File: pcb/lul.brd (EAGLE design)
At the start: 100 x 100 mm, 35 parts, among them IC1 STM32F072C8T6, U1 UG-2864HSWEG01

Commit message: working on pcb
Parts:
- removed S18: ENCODER-SWITCH, SparkFun-Switches:ROTARY_ENC_PLAIN
- removed SJ1, SJ2: (no value), microbuilder:SOLDERJUMPER_REFLOW_NOPASTE
- added IC2: REG1117, clock:SOT223
- added JP1: (no value), pinhead:1X05
- added R1: (no value), clock:0805
- added R10, R11, R12, R13, R14, R15, R16, R21, R5, R6, R7, R8, R9: 330, clock:0805
- added R22, R4: 10k, clock:0805
- added S19, S20, S21, S22: TAC_SWITCHSMD, clock:TACTILE-SWITCH-SMD
- added U$1: N-CHANNEL-MOSFET-BSS138, basicBoard:SOT23-3
- added X1: USB-MICROB, clock:USB-MICROB
- C3, C4, C5, C6, C7, C8, R3: device microbuilder:0805 -> clock:0805
- R17, R18: device SparkFun-Resistors:0603 -> clock:0805
- R19, R20: value 10k -> 330; device SparkFun-Resistors:0603 -> clock:0805
- R2: value 10K -> 10k; device microbuilder:0805 -> clock:0805
- S16: value (none) -> ENCODER-SWITCH; device SparkFun-Switches:CHERRY-MX-LED -> SparkFun-Switches:ROTARY_ENC_PLAIN
- moved S16 110.9 mm to (80.0, 48.0), turned to 180 degrees
- moved R20 102.4 mm to (21.0, 5.50), turned to 90 degrees
- moved R19 85.6 mm to (2.00, 5.50), turned to 90 degrees
- moved U1 13.1 mm to (72.5, 21.9)
- moved SD1 12.0 mm to (82.0, 67.0)
- moved IC1 7.80 mm to (64.0, 66.0)
- moved S17 6.97 mm to (80.0, 86.0), turned to 180 degrees
- moved S3 3.57 mm to (48.0, 86.0)
- moved S6 3.56 mm to (48.0, 67.0)
- moved S9 3.56 mm to (48.0, 48.0)
- moved R2 3.56 mm to (-59.7, -59.4)
- moved S15 3.53 mm to (48.0, 10.0)
- moved S13 2.92 mm to (10.0, 10.0)
- moved S14 2.90 mm to (29.0, 10.0)
- moved S12 2.72 mm to (48.0, 29.0)
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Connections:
- removed net 3.3V: C6.2, C7.2, R17.2, R18.2, R19.2, R20.2, SJ2.1, U1.6, U1.9
- removed net ENCODER_R0: R19.1, S18.B
- removed net ENCODER_R1: R20.1, S18.A
- removed net R_SW: S18.SW+
- removed net VBAT: IC1.1
- removed net VDD: SD1.4
- removed net VDDA: IC1.9
- removed net VDD_1: IC1.24
- removed net VDD_2: IC1.36
- removed net VDD_3: IC1.48
- removed net VSS: SD1.6
- removed net VSSA: IC1.8
- removed net VSS_1: IC1.23
- removed net VSS_2: IC1.35
- removed net VSS_3: IC1.47
- new net +3V3: C6.2, C7.2, IC1.24, IC1.36, IC1.48, IC1.9, IC2.2, IC2.4, R10.2, R11.2, R12.2, R13.2, R14.2, R15.2, R16.2, R17.2, R18.2, R19.2, R20.2, R21.2, R4.2, R5.2, R6.2, R7.2, R8.2, R9.2, S22.3, S22.4, SD1.4, U1.11, U1.6, U1.9
- new net N$10: IC1.16, SD1.7
- new net N$13: IC1.17, SD1.3
- new net N$14: IC1.14, SD1.9
- new net N$15: R5.1, S1.A
- new net N$16: R8.1, S4.A
- new net N$17: R11.1, S7.A
- new net N$18: R14.1, S10.A
- new net N$19: R19.1, S13.A
- new net N$20: R6.1, S2.A
- new net N$21: R9.1, S5.A
- new net N$22: R12.1, S8.A
- new net N$23: R15.1, S11.A
- new net N$24: R20.1, S14.A
- new net N$25: R7.1, S3.A
- new net N$26: R10.1, S6.A
- new net N$27: R13.1, S9.A
- new net N$28: R16.1, S12.A
- new net N$29: R21.1, S15.A
- new net N$30: S1.K, S10.K, S11.K, S12.K, S13.K, S14.K, S15.K, S2.K, S3.K, S4.K, S5.K, S6.K, S7.K, S8.K, S9.K, U$1.3
- new net N$31: R22.2, U$1.1
- new net N$8: IC1.15, SD1.5
- new net N$9: IC1.7, R4.1, S21.1, S21.2
- new net SD_CS: IC1.18, SD1.2
- new net USB_DN: IC1.32, X1.D-
- new net USB_DP: IC1.33, X1.D+
- net D1/MOSI/SDA1_3.3V: now also U1.20; no longer SJ1.1
- net GND: now also IC1.1, IC1.23, IC1.35, IC1.47, IC1.8, IC2.1, R22.1, S1.S1, S10.S1, S11.S1, S12.S1, S13.S1, S14.S1, S15.S1, S2.S1, S21.3, S21.4, S3.S1, S4.S1, S5.S1, S6.S1, S7.S1, S8.S1, S9.S1, SD1.6, SD1.S1, SD1.S2, SD1.S3, SD1.S4, U$1.2, X1.GND, X1.P1, X1.P2, X1.P3, X1.P4, X1.P5, X1.P6; no longer S1.S2, S10.S2, S11.S2, S12.S2, S13.S2, S14.S2, S15.S2, S16.S2, S18.C, S18.SW-, S2.S2, S3.S2, S4.S2, S5.S2, S6.S2, S7.S2, S8.S2, S9.S2
- net N$1: now also IC2.3, X1.VBUS; no longer R2.2, SJ2.2, U1.11
- net N$2: now also IC1.44, R2.2, S22.1, S22.2; no longer SJ1.2, U1.20
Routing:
- net N$30: track 0.00 -> 199.6 mm
- net +3V3: track 0.00 -> 30.0 mm, vias 0 -> 15
- net N$24: track 0.00 -> 6.86 mm
- net N$19: track 0.00 -> 6.86 mm
- net N$29: track 0.00 -> 6.86 mm
- net N$27: track 0.00 -> 4.57 mm
- net N$26: track 0.00 -> 4.57 mm
- net N$28: track 0.00 -> 4.57 mm
- net N$25: track 0.00 -> 4.57 mm
- net N$22: track 0.00 -> 4.57 mm
- net N$21: track 0.00 -> 4.57 mm
- net N$23: track 0.00 -> 4.57 mm
- net N$17: track 0.00 -> 4.57 mm
- net N$16: track 0.00 -> 4.57 mm
- net N$20: track 0.00 -> 4.57 mm
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- added copper zone on layer 16, net +3V3
- added copper zone on layer 1, net GND
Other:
- board size 100 x 100 mm -> 90 x 96 mm

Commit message: routing lulboard
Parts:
- removed R17, R18: 10k, clock:0805
- moved C3 159.4 mm to (72.9, 37.6), turned to 180 degrees
- moved C8 157.3 mm to (87.6, 20.1), turned to 90 degrees
- moved C4 155.9 mm to (76.3, 37.6), turned to 180 degrees
- moved C6 152.6 mm to (79.9, 37.6), turned to 180 degrees
- moved C7 149.3 mm to (83.4, 37.6), turned to 180 degrees
- moved C5 148.4 mm to (87.6, 23.1), turned to 90 degrees
- moved R3 143.2 mm to (87.6, 26.3), turned to 270 degrees
- moved S21 8.00 mm to (64.0, 52.0), turned to 0 degrees
- moved S22 8.00 mm to (64.0, 44.0)
- moved U1 0.06 mm to (72.5, 22.0)
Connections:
- removed net ENCODER_L0: R17.1, S17.B
- removed net ENCODER_L1: R18.1, S17.A
- removed net L_SW: S17.SW+
- new net E1A: IC1.20, S17.A
- new net E1B: IC1.21, S17.B
- new net E1_SW: IC1.19, S17.SW+
- new net E2A: IC1.10, S16.A
- new net E2B: IC1.11, S16.B
- new net E2_SW: IC1.13, S16.SW-
- new net SW10: IC1.43, S10.S2
- new net SW11: IC1.2, S11.S2
- new net SW12: IC1.3, S12.S2
- new net SW13: IC1.4, S13.S2
- new net SW14: IC1.5, S14.S2
- new net SW15: IC1.6, S15.S2
- new net SW4: S4.S2
- new net SW5: IC1.38, S5.S2
- new net SW6: IC1.39, S6.S2
- new net SW7: IC1.40, S7.S2
- new net SW8: IC1.41, S8.S2
- new net SW9: IC1.42, S9.S2
- net +3V3: no longer R17.2, R18.2, S22.4
- net GND: now also S16.C, S16.SW+; no longer S21.3
- net N$2: no longer S22.2
- net N$9: no longer S21.1
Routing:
- net N$30: track 199.6 -> 330.3 mm
- net SW13: track 0.00 -> 91.8 mm
- net SW10: track 0.00 -> 76.6 mm
- net SW14: track 0.00 -> 73.4 mm
- net SW7: track 0.00 -> 55.9 mm
- net SW15: track 0.00 -> 55.2 mm
- net SW11: track 0.00 -> 52.4 mm
- net SW8: track 0.00 -> 36.7 mm
- net SW12: track 0.00 -> 34.0 mm
- net SW5: track 0.00 -> 32.8 mm
- net E1A: track 0.00 -> 30.5 mm
- net E1_SW: track 0.00 -> 27.9 mm
- net E2_SW: track 0.00 -> 26.8 mm
- net E2B: track 0.00 -> 20.3 mm
- net E1B: track 0.00 -> 18.7 mm
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
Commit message: SLMOST FINISHED
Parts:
- removed R1: (no value), clock:0805
- added C1, C10, C2, C9: 0.1uF, clock:0805@1
- added R17: (no value), clock:0805
- added U$8: TEMT6000, ProtoSnap-v14a:TEMT6000-SEN
- C3, C4, C5, C6, C7, C8: device clock:0805 -> clock:0805@1
- moved U$1 191.3 mm to (57.0, 82.5), turned to 90 degrees
- moved R4 172.7 mm to (68.8, 51.8), turned to 315 degrees
- moved R2 161.3 mm to (60.8, 47.8), turned to 180 degrees
- moved R22 91.6 mm to (58.9, 79.8), turned to 180 degrees
- moved R3 10.7 mm to (87.8, 15.6), turned to 180 degrees
- moved C4 6.73 mm to (69.6, 37.5)
- moved C3 6.61 mm to (66.3, 37.5)
- moved C6 6.48 mm to (73.4, 37.7)
- moved C8 6.22 mm to (87.8, 26.3), turned to 180 degrees
- moved C5 1.40 mm to (87.8, 24.5), turned to 180 degrees
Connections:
- removed net CS_3.3V: U1.13
- removed net D0/SCLK/SCK_3.3V: U1.18
- removed net D1/MOSI/SDA1_3.3V: U1.19, U1.20
- removed net DC/SA0_3.3V: U1.15
- removed net N$31: R22.2, U$1.1
- removed net N$9: IC1.7, R4.1, S21.2
- removed net RST_3.3V: U1.14
- new net BACK_LIGHT: IC1.31, R22.2, U$1.1
- new net BUTTON1: IC1.25, S19.1, S19.2
- new net BUTTON2: IC1.22, S20.1, S20.2
- new net LIGHT_SENSOR_OUTPUT: IC1.12, R17.2, U$8.EMITTER
- new net N$32: IC1.37, JP1.1
- new net N$34: IC1.34, JP1.2
- new net RST: IC1.7, R4.1, S21.2, U1.14
- new net SCL: IC1.45, U1.18
- new net SDA: IC1.46, U1.19, U1.20
- new net SW1: IC1.28, S1.S2
- new net SW2: IC1.27, S2.S2
- new net SW3: IC1.26, S3.S2
- new net UART1_TX: IC1.30, JP1.3
- net +3V3: now also C1.2, C10.2, C2.2, C9.2, JP1.4, U$8.COLLECTOR
- net GND: now also C1.1, C10.1, C2.1, C9.1, JP1.5, R17.1, S19.3, S19.4, S20.3, S20.4
- net SW4: now also IC1.29
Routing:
- net BUTTON2: track 0.00 -> 103.2 mm, vias 0 -> 2
- net BUTTON1: track 0.00 -> 94.2 mm, vias 0 -> 2
- net SW1: track 0.00 -> 84.0 mm, vias 0 -> 1
- net SW2: track 0.00 -> 63.3 mm, vias 0 -> 1
- net SW4: track 0.00 -> 58.3 mm, vias 0 -> 2
- net SW3: track 0.00 -> 44.7 mm, vias 0 -> 1
- net USB_DN: track 0.00 -> 22.2 mm
- net USB_DP: track 0.00 -> 22.0 mm
- net +3V3: track 31.8 -> 51.7 mm, vias 16 -> 25
- net N$7: track 0.00 -> 18.9 mm, vias 0 -> 1
- net N$6: track 0.00 -> 18.4 mm, vias 0 -> 1
- net BACK_LIGHT: track 0.00 -> 18.3 mm, vias 0 -> 2
- net N$5: track 0.00 -> 18.1 mm, vias 0 -> 1
- net N$4: track 0.00 -> 17.6 mm, vias 0 -> 1
- net GND: track 0.00 -> 17.6 mm, vias 0 -> 3
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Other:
- outline, holes or cut-outs redrawn

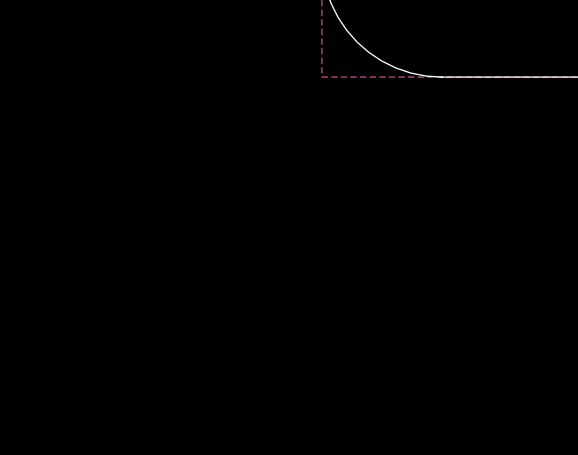
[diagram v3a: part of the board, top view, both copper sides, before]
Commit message: w2812 working, before changing pcb to ws2812
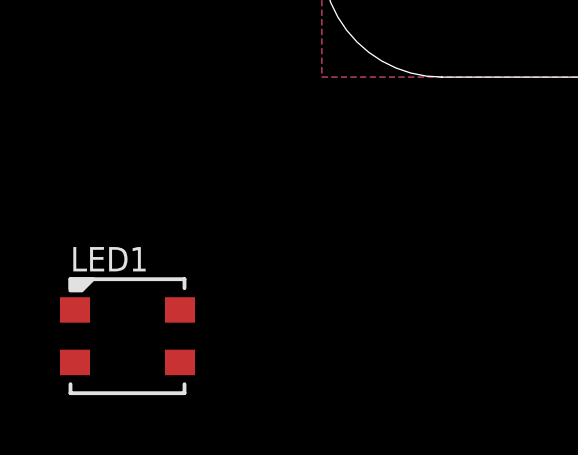
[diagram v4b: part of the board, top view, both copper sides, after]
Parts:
- added LED1: WS2812B3535, adafruit:LED3535
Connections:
- new net VDD: LED1.2
- net GND: now also LED1.4
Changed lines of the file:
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@@
 <element name="U$8" library="ProtoSnap-v14a" package="TEMT6000-SEN" value="TEMT6000" x="69.85" y="56.134" smashed="yes" rot="R315"/>
 <element name="R17" library="clock" package="0805" value="" x="70.739" y="58.547" rot="R135"/>
+<element name="LED1" library="adafruit" package="LED3535" value="WS2812B3535" x="-6.477" y="-8.636"/>
 </elements>
 <signals>
@@
 <contactref element="S20" pad="3"/>
 <contactref element="S20" pad="4"/>
+<contactref element="LED1" pad="4"/>
+<wire x1="84.85" y1="74.9" x2="86.985" y2="88.54" width="0" layer="19" extent="1-1"/>
+<wire x1="75.25" y1="74.025" x2="84.85" y2="74.9" width="0" layer="19" extent="1-1"/>
+<wire x1="70.369" y1="69.977" x2="75.25" y2="74.025" width="0" layer="19" extent="1-1"/>
+<wire x1="68.5" y1="68.25" x2="70.369" y2="69.977" width="0" layer="19" extent="1-1"/>
+<wire x1="69.08" y1="76" x2="70.369" y2="69.977" width="0" layer="19" extent="1-1"/>
+<wire x1="67.1496" y1="82.7394" x2="69.08" y2="76" width="0" layer="19" extent="1-1"/>
+<wire x1="72.507" y1="86" x2="67.1496" y2="82.7394" width="0" layer="19" extent="1-1"/>
+<wire x1="61.75" y1="70.5" x2="68.5" y2="68.25" width="0" layer="19" extent="1-1"/>
+<wire x1="59.944" y1="73.29" x2="61.75" y2="70.5" width="0" layer="19" extent="1-1"/>
+<wire x1="59.828" y1="79.756" x2="59.944" y2="73.29" width="0" layer="19" extent="1-1"/>
+<wire x1="58.023" y1="83.5" x2="59.828" y2="79.756" width="0" layer="19" extent="1-1"/>
+<wire x1="59.5" y1="63.75" x2="61.75" y2="70.5" width="0" layer="19" extent="1-1"/>
+<wire x1="61.25" y1="61.5" x2="59.5" y2="63.75" width="0" layer="19" extent="1-1"/>
+<wire x1="59.436" y1="58.917" x2="61.25" y2="61.5" width="0" layer="19" extent="1-1"/>
+<wire x1="64.75" y1="61.5" x2="61.25" y2="61.5" width="0" layer="19" extent="1-1"/>
+<wire x1="65.278" y1="57.52" x2="64.75" y2="61.5" width="0" layer="19" extent="1-1"/>
+<wire x1="71.37539375" y1="57.910603125" x2="65.278" y2="57.52" width="0" layer="19" extent="1-1"/>
+<wire x1="75.25" y1="59.04" x2="71.37539375" y2="57.910603125" width="0" layer="19" extent="1-1"/>
+<wire x1="74.38" y1="63.7" x2="75.25" y2="59.04" width="0" layer="19" extent="1-1"/>
+<wire x1="66.794" y1="50.095" x2="65.278" y2="57.52" width="0" layer="19" extent="1-1"/>
+<wire x1="61.733" y1="47.752" x2="66.794" y2="50.095" width="0" layer="19" extent="1-1"/>
+<wire x1="72.507" y1="48" x2="66.794" y2="50.095" width="0" layer="19" extent="1-1"/>
+<wire x1="66.5" y1="91.8" x2="72.507" y2="86" width="0" layer="19" extent="1-1"/>
+<wire x1="67.5" y1="94.5" x2="66.5" y2="91.8" width="0" layer="19" extent="1-1"/>
+<wire x1="65" y1="94.5" x2="67.5" y2="94.5" width="0" layer="19" extent="1-1"/>
+<wire x1="63" y1="94.5" x2="65" y2="94.5" width="0" layer="19" extent="1-1"/>
+<wire x1="60.5" y1="94.5" x2="63" y2="94.5" width="0" layer="19" extent="1-1"/>
+<wire x1="62.7" y1="91.85" x2="63" y2="94.5" width="0" layer="19" extent="1-1"/>
+<wire x1="61.5" y1="91.8" x2="62.7" y2="91.85" width="0" layer="19" extent="1-1"/>
+<wire x1="84.85" y1="59.1" x2="75.25" y2="59.04" width="0" layer="19" extent="1-1"/>
+<wire x1="74.306" y1="37.719" x2="72.507" y2="48" width="0" layer="19" extent="1-1"/>
+<wire x1="84.339" y1="37.592" x2="74.306" y2="37.719" width="0" layer="19" extent="1-1"/>
+<wire x1="86.985" y1="45.46" x2="84.339" y2="37.592" width="0" layer="19" extent="1-1"/>
+<wire x1="88.657" y1="26.289" x2="84.339" y2="37.592" width="0" layer="19" extent="1-1"/>
+<wire x1="88.657" y1="24.511" x2="88.657" y2="26.289" width="0" layer="19" extent="1-1"/>
+<wire x1="82.65" y1="20.8" x2="88.657" y2="24.511" width="0" layer="19" extent="1-16"/>
+<wire x1="88.657" y1="15.621" x2="82.677" y2="18.161" width="0" layer="19" extent="1-1"/>
+<wire x1="82.794" y1="5.595" x2="88.657" y2="15.621" width="0" layer="19" extent="1-1"/>
+<wire x1="77.206" y1="5.595" x2="82.794" y2="5.595" width="0" layer="19" extent="1-1"/>
+<wire x1="67.794" y1="5.595" x2="77.206" y2="5.595" width="0" layer="19" extent="1-1"/>
+<wire x1="62.206" y1="5.595" x2="67.794" y2="5.595" width="0" layer="19" extent="1-1"/>
+<wire x1="70.05" y1="20.8" x2="81.95" y2="20.8" width="0" layer="19" extent="16-16"/>
+<wire x1="62.35" y1="20.8" x2="67.25" y2="20.8" width="0" layer="19" extent="16-16"/>
+<wire x1="44.19" y1="88.54" x2="58.023" y2="83.5" width="0" layer="19" extent="1-1"/>
+<wire x1="44.19" y1="69.54" x2="59.944" y2="73.29" width="0" layer="19" extent="1-1"/>
+<wire x1="44.19" y1="50.54" x2="59.436" y2="58.917" width="0" layer="19" extent="1-1"/>
+<wire x1="25.19" y1="88.54" x2="44.19" y2="88.54" width="0" layer="19" extent="1-1"/>
+<wire x1="6.19" y1="88.54" x2="25.19" y2="88.54" width="0" layer="19" extent="1-1"/>
+<wire x1="25.19" y1="69.54" x2="44.19" y2="69.54" width="0" layer="19" extent="1-1"/>
+<wire x1="6.19" y1="69.54" x2="6.19" y2="88.54" width="0" layer="19" extent="1-1"/>
+<wire x1="44.19" y1="31.54" x2="44.19" y2="50.54" width="0" layer="19" extent="1-1"/>
+<wire x1="25.19" y1="50.54" x2="44.19" y2="50.54" width="0" layer="19" extent="1-1"/>
+<wire x1="6.19" y1="50.54" x2="6.19" y2="69.54" width="0" layer="19" extent="1-1"/>
+<wire x1="25.19" y1="31.54" x2="44.19" y2="31.54" width="0" layer="19" extent="1-1"/>
+<wire x1="44.19" y1="12.54" x2="62.35" y2="18.168" width="0" layer="19" extent="16-16"/>
+<wire x1="6.19" y1="31.54" x2="6.19" y2="50.54" width="0" layer="19" extent="1-1"/>
+<wire x1="25.19" y1="12.54" x2="25.19" y2="31.54" width="0" layer="19" extent="1-1"/>
+<wire x1="6.19" y1="12.54" x2="6.19" y2="31.54" width="0" layer="19" extent="1-1"/>
+<wire x1="-4.727" y1="-7.761" x2="6.19" y2="12.54" width="0" layer="19" extent="1-1"/>
 </signal>
 <signal name="E1B">
@@
 <wire x1="67.794" y1="9.405" x2="62.206" y2="9.405" width="0.2032" layer="1"/>
 </signal>
+<signal name="VDD">
+<contactref element="LED1" pad="2"/>
+</signal>
 </signals>

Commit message: before rotating
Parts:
- removed R10, R11, R12, R13, R14, R15, R16, R19, R20, R21, R5, R6, R7, R8, R9: 330, clock:0805
- removed R22: 10k, clock:0805
- removed U$1: N-CHANNEL-MOSFET-BSS138, basicBoard:SOT23-3
- S1, S10, S11, S12, S13, S14, S15, S2, S3, S4, S5, S6, S7, S8, S9: value (none) -> MOMENTARY-SWITCH-SPST-LED-PTH-CHERRY; device SparkFun-Switches:CHERRY-MX-LED -> lul:CHERRY-MX-LED
- moved LED1 7.50 mm to (-13.2, -5.33)
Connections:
- removed net N$15: R5.1, S1.A
- removed net N$16: R8.1, S4.A
- removed net N$17: R11.1, S7.A
- removed net N$18: R14.1, S10.A
- removed net N$19: R19.1, S13.A
- removed net N$20: R6.1, S2.A
- removed net N$21: R9.1, S5.A
- removed net N$22: R12.1, S8.A
- removed net N$23: R15.1, S11.A
- removed net N$24: R20.1, S14.A
- removed net N$25: R7.1, S3.A
- removed net N$26: R10.1, S6.A
- removed net N$27: R13.1, S9.A
- removed net N$28: R16.1, S12.A
- removed net N$29: R21.1, S15.A
- removed net N$30: S1.K, S10.K, S11.K, S12.K, S13.K, S14.K, S15.K, S2.K, S3.K, S4.K, S5.K, S6.K, S7.K, S8.K, S9.K, U$1.3
- net +3V3: no longer R10.2, R11.2, R12.2, R13.2, R14.2, R15.2, R16.2, R19.2, R20.2, R21.2, R5.2, R6.2, R7.2, R8.2, R9.2
- net BACK_LIGHT: no longer R22.2, U$1.1
- net GND: no longer R22.1, U$1.2
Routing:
- net N$30: track 340.2 -> 0.00 mm
- net +3V3: track 51.7 -> 21.7 mm, vias 25 -> 10
- net BACK_LIGHT: track 18.3 -> 0.00 mm, vias 2 -> 0
- net N$24: track 6.86 -> 0.00 mm
- net N$19: track 6.86 -> 0.00 mm
- net N$29: track 6.86 -> 0.00 mm
- net N$27: track 4.57 -> 0.00 mm
- net N$26: track 4.57 -> 0.00 mm
- net N$28: track 4.57 -> 0.00 mm
- net N$25: track 4.57 -> 0.00 mm
- net N$22: track 4.57 -> 0.00 mm
- net N$21: track 4.57 -> 0.00 mm
- net N$23: track 4.57 -> 0.00 mm
- net N$17: track 4.57 -> 0.00 mm
- net N$16: track 4.57 -> 0.00 mm
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
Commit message: routing finished
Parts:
- added C11, C12, C13, C14, C15, C16, C17, C18, C19, C20, C21, C22, C23, C24, C25, C26: 0.1uF, clock:0805@1
- added C27: (no value), clock:C1210
- added IC3: 74LVC1G125DBV, 74xx-little-de:SOT23-5
- added LED10, LED11, LED12, LED13, LED14, LED15, LED2, LED3, LED4, LED5, LED6, LED7, LED8, LED9: WS2812B3535, lul:LED3535
- added R1, R5: 10k, clock:0805
- added R6: 300, clock:0805
- LED1: device adafruit:LED3535 -> lul:LED3535
- moved LED1 99.1 mm to (10.0, 91.0), turned to 180 degrees
- moved C7 30.2 mm to (57.8, 21.7), turned to 270 degrees
- moved C6 20.9 mm to (86.9, 21.7), turned to 270 degrees
- turned S1 to 180 degrees
- turned S10 to 180 degrees
- turned S11 to 180 degrees
- turned S12 to 180 degrees
- turned S13 to 180 degrees
- turned S14 to 180 degrees
- turned S15 to 180 degrees
- turned S2 to 180 degrees
- turned S3 to 180 degrees
- turned S4 to 180 degrees
- turned S5 to 180 degrees
- turned S6 to 180 degrees
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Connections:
- removed net BACK_LIGHT: IC1.31
- removed net N$13: IC1.17, SD1.3
- removed net VDD: LED1.2
- new net LED_DATA_EN: IC1.31, IC3.1, R5.1
- new net N$15: LED1.1, LED2.3
- new net N$16: IC1.17, R6.1
- new net N$17: LED1.3, LED4.1
- new net N$18: LED4.3, LED5.1
- new net N$19: LED5.3, LED6.1
- new net N$20: LED6.3, LED9.1
- new net N$21: LED8.1, LED9.3
- new net N$22: LED7.1, LED8.3
- new net N$23: LED10.1, LED7.3
- new net N$24: LED10.3, LED11.1
- new net N$25: LED11.3, LED12.1
- new net N$26: LED12.3, LED15.1
- new net N$27: LED14.1, LED15.3
- new net N$28: LED13.1, LED14.3
- new net N$29: IC3.4, LED3.1, R1.2
- new net N$9: LED2.1, LED3.3
- new net SPI_MOSI: IC3.2, R6.2, SD1.3
- net +3V3: now also C11.2, C12.2, C13.2, C14.2, C15.2, C16.2, C17.2, C18.2, C19.2, C20.2, C21.2, C22.2, C23.2, C24.2, C25.2, C26.2, C27.1, IC3.5, LED1.2, LED10.2, LED11.2, LED12.2, LED13.2, LED14.2, LED15.2, LED2.2, LED3.2, LED4.2, LED5.2, LED6.2, LED7.2, LED8.2, LED9.2, R5.2
- net GND: now also C11.1, C12.1, C13.1, C14.1, C15.1, C16.1, C17.1, C18.1, C19.1, C20.1, C21.1, C22.1, C23.1, C24.1, C25.1, C26.1, C27.2, IC3.3, LED10.4, LED11.4, LED12.4, LED13.4, LED14.4, LED15.4, LED2.4, LED3.4, LED4.4, LED5.4, LED6.4, LED7.4, LED8.4, LED9.4, R1.1, S1.S2, S10.S2, S11.S2, S12.S2, S13.S2, S14.S2, S15.S2, S2.S2, S3.S2, S4.S2, S5.S2, S6.S2, S7.S2, S8.S2, S9.S2; no longer S1.S1, S10.S1, S11.S1, S12.S1, S13.S1, S14.S1, S15.S1, S2.S1, S3.S1, S4.S1, S5.S1, S6.S1, S7.S1, S8.S1, S9.S1
- net SW1: now also IC1.26, S1.S1; no longer IC1.28, S1.S2
- net SW10: now also S10.S1; no longer S10.S2
- net SW11: now also S11.S1; no longer S11.S2
- net SW12: now also S12.S1; no longer S12.S2
- net SW13: now also S13.S1; no longer S13.S2
- net SW14: now also S14.S1; no longer S14.S2
- net SW15: now also S15.S1; no longer S15.S2
- net SW2: now also S2.S1; no longer S2.S2
- net SW3: now also IC1.28, S3.S1; no longer IC1.26, S3.S2
- net SW4: now also S4.S1; no longer S4.S2
- net SW5: now also S5.S1; no longer S5.S2
- net SW6: now also S6.S1; no longer S6.S2
- net SW7: now also S7.S1; no longer S7.S2
- net SW8: now also S8.S1; no longer S8.S2
- net SW9: now also S9.S1; no longer S9.S2
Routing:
- net +3V3: track 21.7 -> 100.8 mm, vias 10 -> 30
- net SDA: track 0.70 -> 62.4 mm, vias 0 -> 1
- net SCL: track 0.00 -> 57.2 mm, vias 0 -> 1
- net SPI_MOSI: track 0.00 -> 40.0 mm, vias 0 -> 2
- net RST: track 10.7 -> 44.5 mm, vias 0 -> 1
- net N$17: track 0.00 -> 25.2 mm
- net N$26: track 0.00 -> 25.1 mm, vias 0 -> 2
- net N$20: track 0.00 -> 25.1 mm, vias 0 -> 2
- net N$23: track 0.00 -> 24.9 mm
- net N$2: track 0.00 -> 24.8 mm, vias 0 -> 2
- net LED_DATA_EN: track 0.00 -> 23.7 mm, vias 0 -> 2
- net N$9: track 0.00 -> 16.3 mm
- net N$18: track 0.00 -> 16.3 mm
- net N$28: track 0.00 -> 16.2 mm
- net N$27: track 0.00 -> 16.2 mm
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
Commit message: seemingly finished
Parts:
- removed C26: 0.1uF, clock:0805@1
- U1: device microbuilder:UG-2864HSWEG01_0.96IN_WRAPAROUND -> lul:UG-2864HSWEG01_0.96IN_WRAPAROUND
- moved C27 5.13 mm to (69.3, 83.7), turned to 270 degrees
- moved R1 4.30 mm to (57.9, 92.7), turned to 270 degrees
- moved C3 1.52 mm to (66.3, 39.0)
- moved C4 1.52 mm to (69.6, 39.0)
- moved S19 1.02 mm to (80.0, 8.52)
- moved S20 1.02 mm to (65.0, 8.52)
- moved IC2 0.89 mm to (63.1, 85.0)
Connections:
- net +3V3: no longer C26.2
- net GND: no longer C26.1
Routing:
- net E1A: track 30.5 -> 25.6 mm
- net N$7: track 18.9 -> 20.4 mm
- net N$6: track 18.4 -> 20.0 mm
- net N$5: track 18.1 -> 19.6 mm
- net N$4: track 17.6 -> 19.2 mm
- net SW10: track 82.3 -> 81.3 mm
- net +3V3: track 100.8 -> 100.3 mm, vias 30 -> 29
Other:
- outline, holes or cut-outs redrawn
- board text added: "+"
- board text added: "-"
- board text added: "2017"
- board text added: "3V3"
- board text added: "CLK"
- board text added: "DFU"
- board text added: "DIO"
- board text added: "GND"
- board text added: "RST"
- board text added: "TX"
- board text added: "dekuNukem"
- board text added: "tangentbord"
